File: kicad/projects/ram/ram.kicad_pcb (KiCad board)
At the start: 2 copper layers, 203.2 x 97.8 mm, 45 parts, among them J1 peripheral_addr_bus_connector, J2 peripheral_aux_connector, J3 peripheral_membank_connector, J5 Conn_02x16_Odd_Even, U1 74HC02, U10 74HC30, U11 74HC32, U12 74HC08, U2 74HC08, U3 74HC123, U4 74HC04, U5 74HC245, U6 74HC245, U7 628128_DIP32_SSOP32, U8 628128_DIP32_SSOP32, U9 74HC30

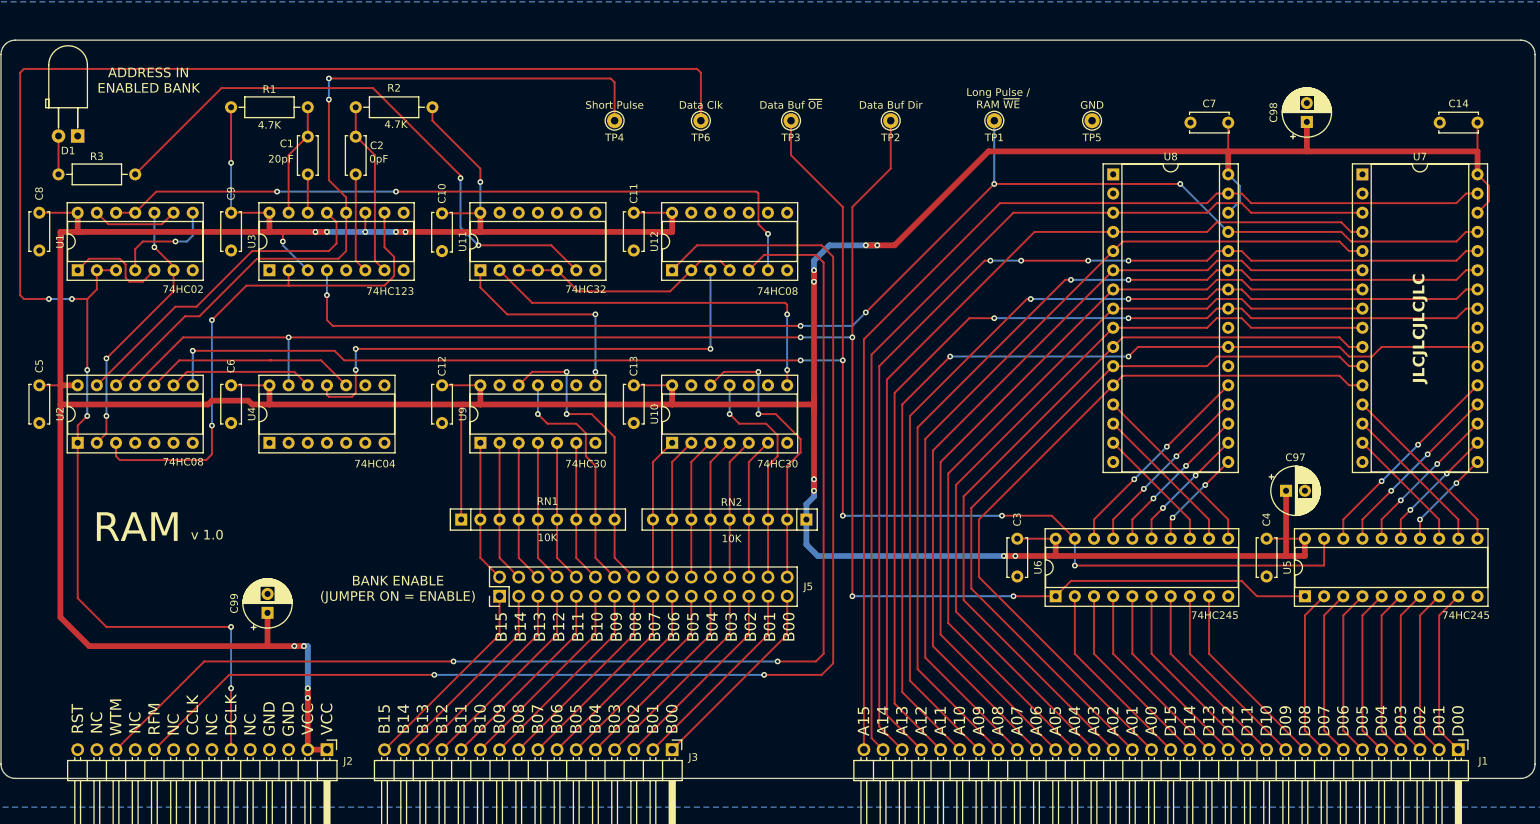
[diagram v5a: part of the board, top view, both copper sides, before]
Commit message: RAM converted to single line rfm wtm.
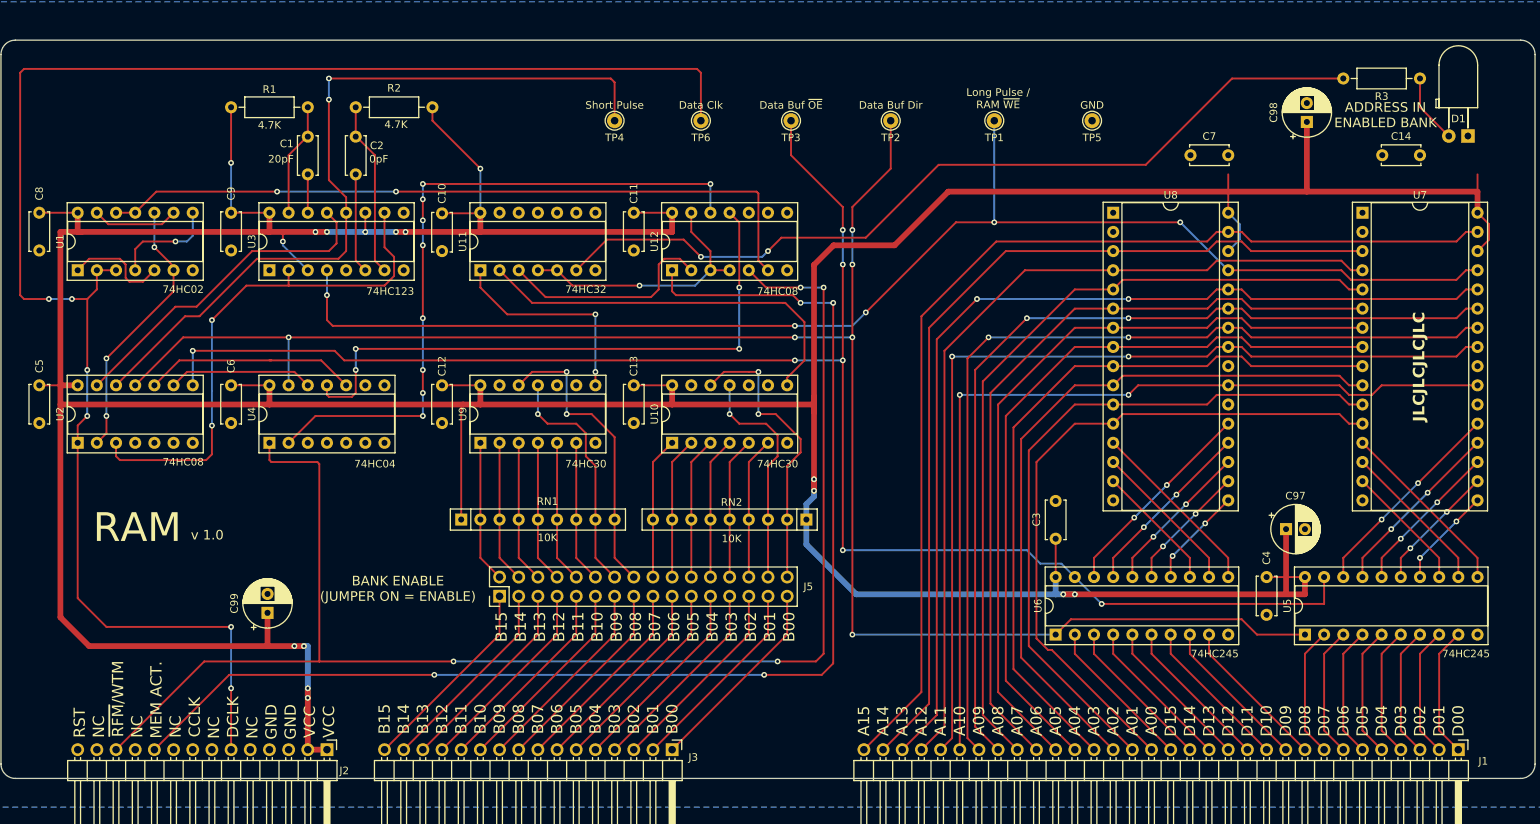
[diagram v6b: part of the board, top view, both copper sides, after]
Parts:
- moved D1 184.2 mm to (245.1, 63.5)
- moved R3 180.8 mm to (238.8, 55.9), turned to 180 degrees
- moved C14 8.76 mm to (233.8, 66.0)
- moved C3 5.08 mm to (190.5, 116.8), turned to 90 degrees
- moved C4 5.08 mm to (218.4, 121.9)
- moved C97 5.08 mm to (221.0, 115.6)
- moved U5 5.08 mm to (223.5, 129.5)
- moved U6 5.08 mm to (190.5, 129.5)
- moved U7 5.08 mm to (231.1, 73.7)
- moved U8 5.08 mm to (198.1, 73.7)
- moved C7 4.32 mm to (208.4, 66.0)
- turned J2 to 0 degrees
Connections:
- net /RFM renamed /MEM_ACT
- J2 pad 12: /WTM -> /RFM_WTM
- U11 pad 3: Net-(U11-Pad3) -> /BANK_ADDRESSED
- U11 pad 4: Net-(U11-Pad3) -> Net-(U11-Pad4)
- U11 pad 5: Net-(U11-Pad3) -> Net-(U11-Pad4)
- U12 pad 11: unconnected-(U12-Pad11) -> /ADDRESSED_RFM
- U12 pad 12: GND -> Net-(U12-Pad12)
- U12 pad 13: GND -> Net-(U11-Pad4)
- U12 pad 2: Net-(U11-Pad3) -> /BANK_ADDRESSED
- U12 pad 3: /ADDRESSED_RFM -> Net-(U11-Pad4)
- U12 pad 4: Net-(U11-Pad3) -> Net-(U11-Pad4)
- U12 pad 5: /WTM -> /RFM_WTM
- U4 pad 1: GND -> /RFM_WTM
- U4 pad 2: unconnected-(U4-Pad2) -> Net-(U12-Pad12)
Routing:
- net /RFM_WTM: track 0.00 -> 193.6 mm, vias 0 -> 4
- net /WTM: track 162.0 -> 0.00 mm, vias 2 -> 0
- net Net-(U12-Pad12): track 0.00 -> 91.9 mm, vias 0 -> 9
- net Net-(R3-Pad2): track 77.2 -> 114.0 mm
- net Net-(U11-Pad4): track 0.00 -> 35.8 mm, vias 0 -> 1
- net Net-(U11-Pad3): track 31.2 -> 0.00 mm
- net /BANK_ADDRESSED: track 0.00 -> 29.0 mm
- net /ADDR_BUS_10: track 129.3 -> 117.1 mm
- net /ADDRESSED_RFM: track 68.6 -> 80.6 mm, vias 3 -> 4
- net /ADDR_BUS_11: track 132.7 -> 123.9 mm
- net /ADDR_BUS_09: track 131.2 -> 122.7 mm
- net /ADDR_BUS_06: track 113.1 -> 104.7 mm
- net /ADDR_BUS_03: track 106.2 -> 97.7 mm
- net /ADDR_BUS_02: track 103.8 -> 95.4 mm
- net /ADDR_BUS_08: track 130.9 -> 122.5 mm
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
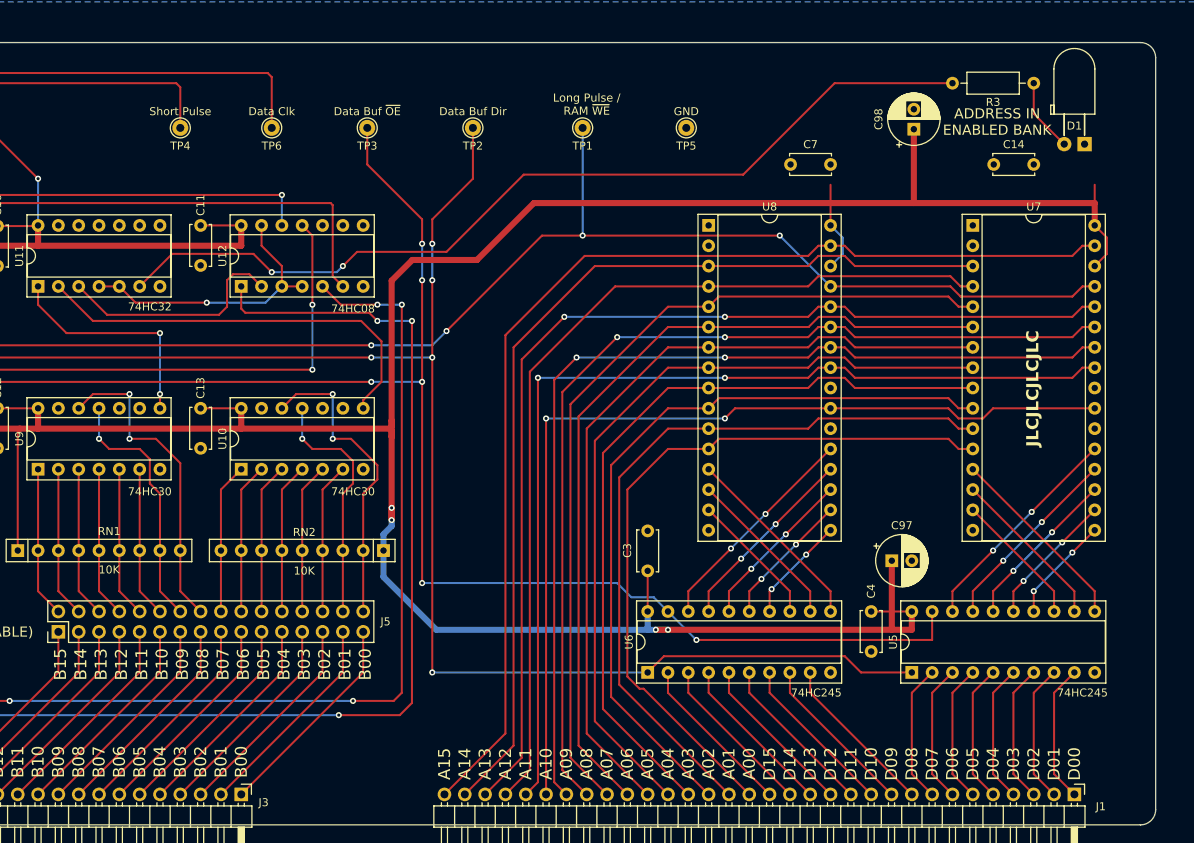
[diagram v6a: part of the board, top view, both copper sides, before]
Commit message: LED positioning tidy up.
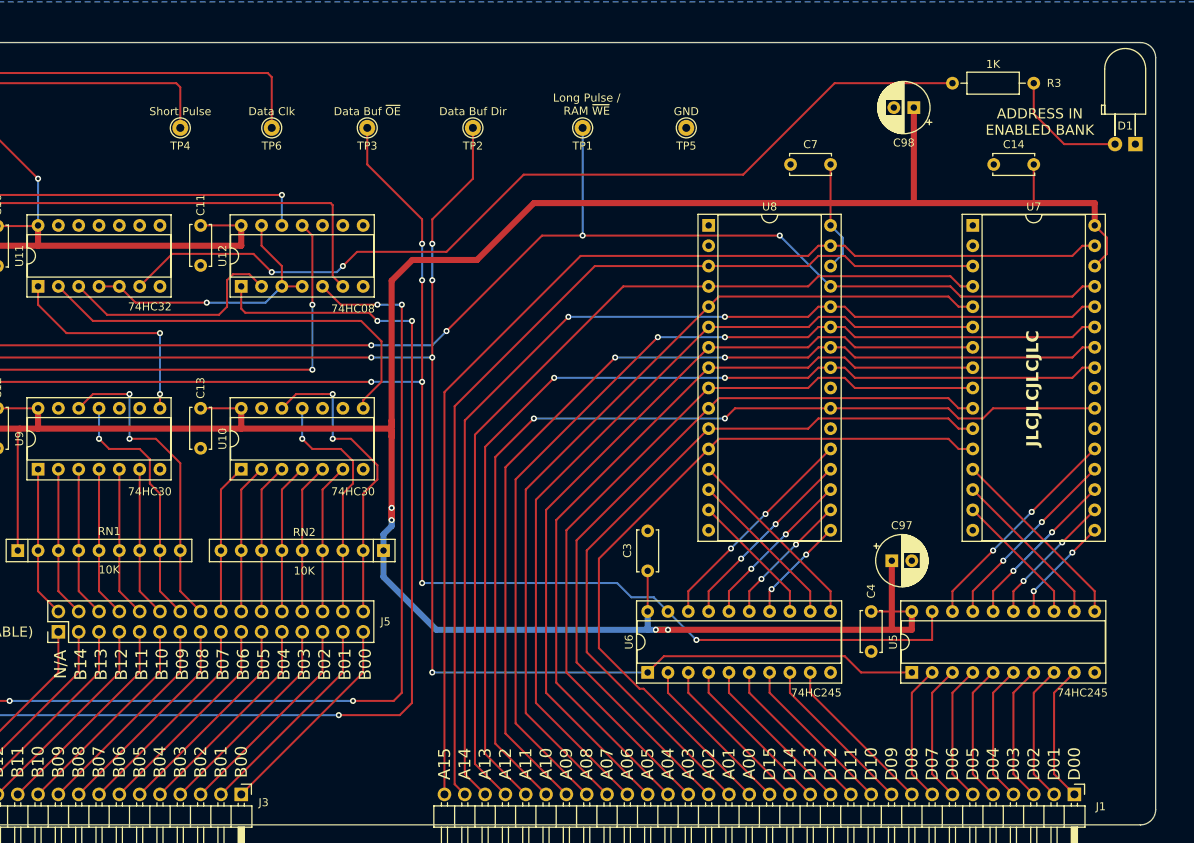
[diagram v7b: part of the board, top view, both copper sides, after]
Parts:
- moved D1 6.35 mm to (251.5, 63.5)
- moved C98 2.71 mm to (223.8, 58.9), turned to 180 degrees
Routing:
- net VCC: track 666.2 -> 674.0 mm
- net Net-(D1-A): track 9.20 -> 15.5 mm
- net /ADDR_BUS_10: track 117.1 -> 123.3 mm
- net /ADDR_BUS_11: track 123.9 -> 126.9 mm
- net /ADDR_BUS_12: track 114.9 -> 117.5 mm
- net /ADDR_BUS_09: track 122.7 -> 125.0 mm
- net /ADDR_BUS_08: track 122.5 -> 124.4 mm
- net /ADDR_BUS_13: track 131.7 -> 133.5 mm
- net /ADDR_BUS_07: track 107.1 -> 108.7 mm
- net /ADDR_BUS_06: track 104.7 -> 106.2 mm
- net /ADDR_BUS_05: track 102.4 -> 103.6 mm
- net /ADDR_BUS_14: track 121.1 -> 122.1 mm
- net /ADDR_BUS_04: track 100.1 -> 101.1 mm
- net /ADDR_BUS_03: track 97.7 -> 98.5 mm
- net /ADDR_BUS_02: track 95.4 -> 96.0 mm

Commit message: RAM tech checks complete.
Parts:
- added R4: 10K, Resistor_THT:R_Axial_DIN0207_L6.3mm_D2.5mm_P10.16mm_Horizontal, F.Cu at (170.7, 66.5)
- C97, C98, C99: value C_Polarized -> 33uF
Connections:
- C1 pad 1: Net-(U3A-Cext) -> GND
- C2 pad 1: Net-(U3B-Cext) -> GND
- U11 pad 10: GND -> /ADDRESSED_RFM
- U11 pad 8: unconnected-(U11-Pad8) -> Net-(U11-Pad8)
- U11 pad 9: GND -> /DATA_BUF_DIR
- U2 pad 10: Net-(U2-Pad10) -> GND
- U2 pad 8: /DATA_BUF_~{OE} -> unconnected-(U2-Pad8)
- U2 pad 9: Net-(U2-Pad9) -> GND
- U3 pad 14: Net-(U3A-Cext) -> GND
- U3 pad 6: Net-(U3B-Cext) -> GND
- U4 pad 10: Net-(U2-Pad10) -> /DATA_BUF_~{OE}
- U4 pad 11: /ADDRESSED_RFM -> Net-(U11-Pad8)
- U4 pad 12: Net-(U2-Pad9) -> unconnected-(U4-Pad12)
- U4 pad 13: /DATA_BUF_DIR -> GND
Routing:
- net Net-(U11-Pad8): track 0.00 -> 53.1 mm, vias 0 -> 3
- net /ADDRESSED_RFM: track 80.6 -> 33.5 mm, vias 4 -> 2
- net /DATA_BUF_DIR: track 235.8 -> 276.7 mm
- net Net-(U2-Pad10): track 28.4 -> 0.00 mm
- net /DATA_CLK: track 220.7 -> 196.6 mm
- net /DATA_BUF_~{OE}: track 221.2 -> 197.1 mm, vias 7 -> 6
- net Net-(U2-Pad9): track 19.3 -> 0.00 mm
- net GND: track 0.00 -> 18.3 mm
- net Net-(U3B-Cext): track 13.2 -> 0.00 mm
- net /RFM_WTM: track 193.6 -> 187.1 mm
- net Net-(U3A-Cext): track 5.08 -> 0.00 mm
- net /MEM_ACT: track 167.2 -> 163.7 mm
- net Net-(U3B-~{Q}): track 104.8 -> 101.8 mm
- net Net-(U9A-~{Y}): track 28.4 -> 27.1 mm
- net /ADDRESSED_WTM: track 97.0 -> 96.0 mm
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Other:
- board text added: "(Active Low)"
- board text added: "MEMORY ACCESS"
- board text added: "SRAM"
- board text removed: "ADDRESS IN ENABLED BANK"
